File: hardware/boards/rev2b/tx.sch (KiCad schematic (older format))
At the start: 59 parts, among them J3 SMA, Q2 RE1C002UN, T1 uwave, T2 uwave, U12 ADF4158, U13 TLV172DCK, U14 PAT1220-C-3DB, U15 HMC431, U16 PD4859J5050S2HF, U17 PAT1220-C-5DB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

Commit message: rev2b pcb: replace wilkinson divider with power splitter
Closes #4.
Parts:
- removed R47: 100, fmcw_v5:R_0603b, symbol Device:R
- removed U14: PAT1220-C-3DB, RF_Converter:RF_Attenuator_Susumu_PAT1220, symbol RF:PAT1220-C-3DB
- removed U16: PD4859J5050S2HF, RF_Converter:Anaren_0805_2012Metric-6, symbol RF:PD4859J5050S2HF
- added U14: PS2012GT2-R50, fmcw_v5:Susumu_PS2012GT2-R50, symbol fmcw:PS2012GT2-R50
- U17: value PAT1220-C-5DB -> PAT1220-C-2DB; symbol RF:PAT1220-C-5DB -> RF:PAT1220-C-2DB; MFN PAT1220-C-5DB-T5 -> PAT1220-C-2DB-T5
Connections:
- net GND: now also U14.4 (GND)
- net at U15.16 (RFOUT): now also U14.1 (In)
- net at C112.1: now also T1.1, T2.1, U14.3 (Out)
- net at U17.1: now also U14.2 (Out)
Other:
- note removed: "-1 dBm"
- moved on the sheet: T2
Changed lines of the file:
@@
 Connection ~ 3050 5550
 Connection ~ 6800 6000
-Connection ~ 9950 5800
-Connection ~ 9950 6200
 Connection ~ 8150 5050
 Connection ~ 6200 5550
@@
 Connection ~ 8150 6400
 Connection ~ 9300 7450
-Connection ~ 9950 7150
 NoConn ~ 2900 5800
 NoConn ~ 12500 4800
@@
 	4000 6700 4000 6650
 Wire Wire Line
-	4400 7450 7400 7450
-Wire Wire Line
 	4450 4000 4300 4000
 Wire Wire Line
@@
 	7750 6400 8150 6400
 Wire Wire Line
-	7800 7850 7800 7900
-Wire Wire Line
 	7850 3800 7900 3800
 Wire Wire Line
@@
 	8200 5250 8150 5250
 Wire Wire Line
-	8200 7450 9300 7450
-Wire Wire Line
 	8250 3550 8250 3600
 Wire Wire Line
@@
 	9300 7450 9300 7550
 Wire Wire Line
-	9300 7450 9950 7450
-Wire Wire Line
-	9400 6350 9400 6300
+	9300 7450 10150 7450
 Wire Wire Line
 	9450 3550 9450 2900
@@
 	9550 3550 9450 3550
 Wire Wire Line
-	9800 5900 9850 5900
-Wire Wire Line
-	9800 6100 9850 6100
-Wire Wire Line
 	9850 4100 9950 4100
 Wire Wire Line
-	9850 5800 9850 5900
-Wire Wire Line
-	9850 6100 9850 6200
-Wire Wire Line
-	9850 6200 9950 6200
-Wire Wire Line
 	9950 3550 9850 3550
 Wire Wire Line
@@
 	9950 4450 9800 4450
 Wire Wire Line
-	9950 5100 9950 5800
-Wire Wire Line
 	9950 5100 10000 5100
 Wire Wire Line
-	9950 5800 9850 5800
-Wire Wire Line
-	9950 5800 9950 5850
-Wire Wire Line
-	9950 6150 9950 6200
-Wire Wire Line
-	9950 6200 9950 7150
-Wire Wire Line
-	9950 7150 9950 7450
+	10150 7150 10150 7450
 Wire Wire Line
 	10050 4100 10050 4300
@@
 Text Notes 1200 4700 0    50   ~ 0
 32 (23) mA
-Text Notes 3200 7450 0    50   ~ 0
--4 dBm
 Text Notes 4900 4250 2    50   ~ 0
 5 mA
@@
 +2dBm
 Text Notes 8850 7450 0    50   ~ 0
--1 dBm
+-4 dBm
 Text Notes 9000 4000 0    50   ~ 0
 2.85V
 Text Notes 9600 5400 0    50   ~ 0
--1 dBm
+-4 dBm
 Text Notes 9900 2050 0    50   ~ 0
 800 (300) mA
@@
 $EndComp
 $Comp
-L power:GND #PWR0115
-U 1 1 5CF6E09E
-P 7800 7900
-F 0 "#PWR0115" H 7800 7650 50  0001 C CNN
-F 1 "GND" H 7805 7727 50  0000 C CNN
-F 2 "" H 7800 7900 50  0001 C CNN
-F 3 "" H 7800 7900 50  0001 C CNN
-	1    7800 7900
-	1    0    0    -1
-$EndComp
-$Comp
 L power:GND #PWR0101
 U 1 1 5C609590
@@
 L power:GND #PWR0121
 U 1 1 5CE085DA
-P 9400 6350
-F 0 "#PWR0121" H 9400 6100 50  0001 C CNN
-F 1 "GND" H 9405 6177 50  0000 C CNN
-F 2 "" H 9400 6350 50  0001 C CNN
-F 3 "" H 9400 6350 50  0001 C CNN
-	1    9400 6350
+P 9200 6450
+F 0 "#PWR0121" H 9200 6200 50  0001 C CNN
+F 1 "GND" H 9205 6277 50  0000 C CNN
+F 2 "" H 9200 6450 50  0001 C CNN
+F 3 "" H 9200 6450 50  0001 C CNN
+	1    9200 6450
 	1    0    0    -1
 $EndComp
@@
 $EndComp
 $Comp
-L Device:R R47
-U 1 1 5CFA8165
-P 9950 6000
-F 0 "R47" H 10020 6046 50  0000 L CNN
-F 1 "100" H 10020 5955 50  0000 L CNN
-F 2 "fmcw_v5:R_0603b" V 9880 6000 50  0001 C CNN
-F 3 "~" H 9950 6000 50  0001 C CNN
-F 4 "" H 9950 6000 50  0001 C CNN "MFN"
-	1    9950 6000
-	1    0    0    -1
-$EndComp
-$Comp
 L Device:R R114
 U 1 1 5E79D780
@@
 L fmcw:uwave T2
 U 1 1 5EB0CF7E
-P 10100 7150
-F 0 "T2" V 10055 7278 50  0000 L CNN
-F 1 "uwave" V 10145 7278 50  0000 L CNN
-F 2 "fmcw_v5:uwm_0.38_0.17_90" H 10100 7150 50  0001 C CNN
-F 3 "" H 10100 7150 50  0001 C CNN
-	1    10100 7150
+P 10300 7150
+F 0 "T2" V 10255 7278 50  0000 L CNN
+F 1 "uwave" V 10345 7278 50  0000 L CNN
+F 2 "fmcw_v5:uwm_0.38_0.17_90" H 10300 7150 50  0001 C CNN
+F 3 "" H 10300 7150 50  0001 C CNN
+	1    10300 7150
 	0    1    1    0
 $EndComp
@@
 $EndComp
 $Comp
-L RF:PAT1220-C-3DB U14
-U 1 1 5CF46E5A
-P 7800 7550
-AR Path="/5CF46E5A" Ref="U14"  Part="1"
-AR Path="/59396B94/5CF46E5A" Ref="U14"  Part="1"
-F 0 "U14" H 7800 7939 60  0000 C CNN
-F 1 "PAT1220-C-3DB" H 7800 7833 60  0000 C CNN
-F 2 "RF_Converter:RF_Attenuator_Susumu_PAT1220" H 7800 7550 60  0001 C CNN
-F 3 "" H 7800 7550 60  0000 C CNN
-F 4 "PAT1220-C-3DB-T5" H -3400 2550 50  0001 C CNN "MFN"
-	1    7800 7550
-	1    0    0    -1
-$EndComp
-$Comp
-L RF:PD4859J5050S2HF U16
-U 1 1 5CDBB6B7
-P 9400 6000
-F 0 "U16" H 9400 6367 50  0000 C CNN
-F 1 "PD4859J5050S2HF" H 9400 6276 50  0000 C CNN
-F 2 "RF_Converter:Anaren_0805_2012Metric-6" H 9400 5600 50  0001 C CNN
-F 3 "" H 9150 6250 50  0001 C CNN
-F 4 "PD4859J5050S2HF" H 9400 6000 50  0001 C CNN "MFN"
-	1    9400 6000
-	1    0    0    -1
-$EndComp
-$Comp
-L RF:PAT1220-C-5DB U17
+L RF:PAT1220-C-2DB U17
 U 1 1 54FB1677
 P 10400 5200
@@
 AR Path="/59396B94/54FB1677" Ref="U17"  Part="1"
 F 0 "U17" H 10150 4900 60  0000 C CNN
-F 1 "PAT1220-C-5DB" H 10800 4900 60  0000 C CNN
+F 1 "PAT1220-C-2DB" H 10800 4900 60  0000 C CNN
 F 2 "RF_Converter:RF_Attenuator_Susumu_PAT1220" H 10400 5200 60  0001 C CNN
 F 3 "" H 10400 5200 60  0000 C CNN
-F 4 "PAT1220-C-5DB-T5" H -800 200 50  0001 C CNN "MFN"
+F 4 "PAT1220-C-2DB-T5" H -800 200 50  0001 C CNN "MFN"
 	1    10400 5200
 	1    0    0    -1
@@
 	1    0    0    -1
 $EndComp
+$Comp
+L fmcw:PS2012GT2-R50 U14
+U 1 1 5F5CD072
+P 9400 6000
+F 0 "U14" H 9400 6425 50  0000 C CNN
+F 1 "PS2012GT2-R50" H 9400 6334 50  0000 C CNN
+F 2 "fmcw_v5:Susumu_PS2012GT2-R50" H 9250 5550 50  0001 C CNN
+F 3 "https://www.susumu.co.jp/common/pdf/n_catalog_partition31_en.pdf" H 9350 5650 50  0001 C CNN
+	1    9400 6000
+	1    0    0    -1
+$EndComp
+Connection ~ 10150 7150
+Wire Wire Line
+	9200 6450 9200 6400
+Wire Wire Line
+	4400 7450 9300 7450
+Wire Wire Line
+	10150 5800 9800 5800
+Wire Wire Line
+	10150 5800 10150 7150
+Wire Wire Line
+	9950 6200 9800 6200
+Wire Wire Line
+	9950 5100 9950 6200
 $EndSCHEMATC

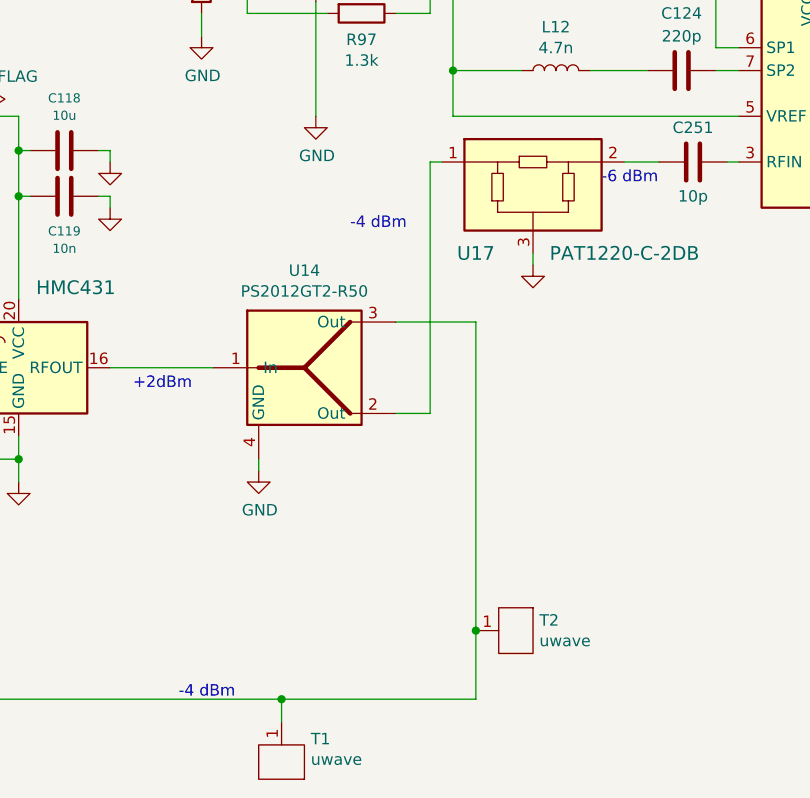
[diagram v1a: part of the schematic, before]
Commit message: rev2 pcb: finish routing traces
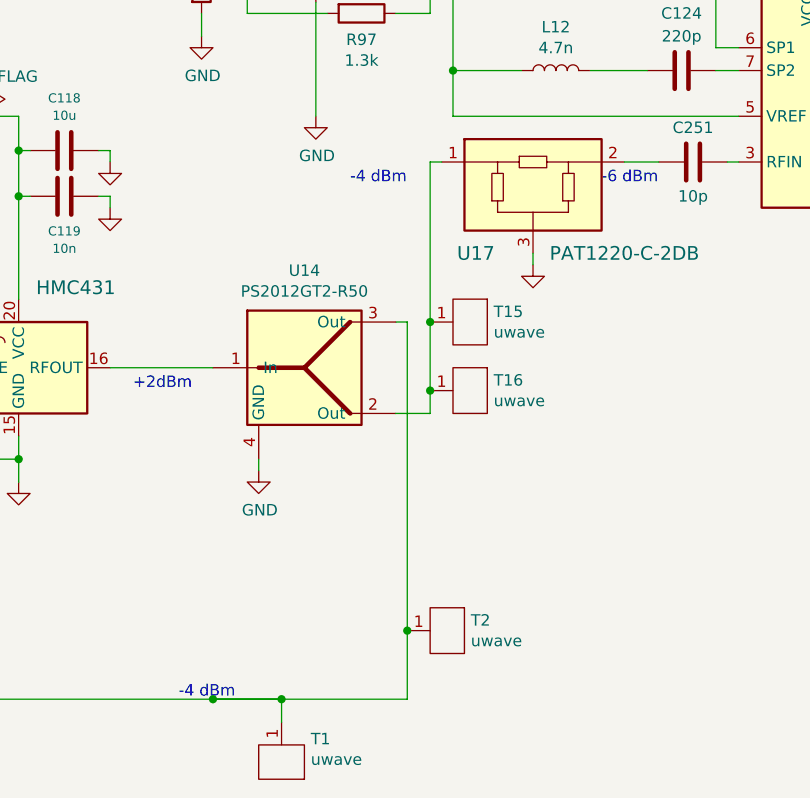
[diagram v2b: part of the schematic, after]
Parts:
- added T15, T16: uwave, fmcw_v5:uwm_0.38_0.17_90, symbol fmcw:uwave
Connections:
- net at U14.2 (Out), U17.1: now also T15.1, T16.1
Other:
- moved on the sheet: T2
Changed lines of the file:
@@
 	9300 7450 9300 7550
 Wire Wire Line
-	9300 7450 10150 7450
-Wire Wire Line
 	9450 3550 9450 2900
 Wire Wire Line
@@
 	9950 5100 10000 5100
 Wire Wire Line
-	10150 7150 10150 7450
+	9850 7150 9850 7450
 Wire Wire Line
 	10050 4100 10050 4300
@@
 Text Notes 9000 4000 0    50   ~ 0
 2.85V
-Text Notes 9600 5400 0    50   ~ 0
+Text Notes 9600 5200 0    50   ~ 0
 -4 dBm
 Text Notes 9900 2050 0    50   ~ 0
@@
 L fmcw:uwave T2
 U 1 1 5EB0CF7E
-P 10300 7150
-F 0 "T2" V 10255 7278 50  0000 L CNN
-F 1 "uwave" V 10345 7278 50  0000 L CNN
-F 2 "fmcw_v5:uwm_0.38_0.17_90" H 10300 7150 50  0001 C CNN
-F 3 "" H 10300 7150 50  0001 C CNN
-	1    10300 7150
+P 10000 7150
+F 0 "T2" V 9955 7278 50  0000 L CNN
+F 1 "uwave" V 10045 7278 50  0000 L CNN
+F 2 "fmcw_v5:uwm_0.38_0.17_90" H 10000 7150 50  0001 C CNN
+F 3 "" H 10000 7150 50  0001 C CNN
+	1    10000 7150
 	0    1    1    0
 $EndComp
@@
 	1    0    0    -1
 $EndComp
-Connection ~ 10150 7150
+Connection ~ 9850 7150
 Wire Wire Line
 	9200 6450 9200 6400
 Wire Wire Line
+	9850 5800 9800 5800
+Wire Wire Line
+	9850 5800 9850 7150
+Wire Wire Line
+	9950 6200 9800 6200
+Wire Wire Line
+	9950 5100 9950 5800
+Connection ~ 9000 7450
+Wire Wire Line
+	9000 7450 9300 7450
+Wire Wire Line
+	9300 7450 9850 7450
+Wire Wire Line
 	4400 7450 9300 7450
-Wire Wire Line
-	10150 5800 9800 5800
-Wire Wire Line
-	10150 5800 10150 7150
-Wire Wire Line
-	9950 6200 9800 6200
-Wire Wire Line
-	9950 5100 9950 6200
+$Comp
+L fmcw:uwave T16
+U 1 1 5F968A43
+P 10100 6100
+F 0 "T16" V 10055 6228 50  0000 L CNN
+F 1 "uwave" V 10145 6228 50  0000 L CNN
+F 2 "fmcw_v5:uwm_0.38_0.17_90" H 10100 6100 50  0001 C CNN
+F 3 "" H 10100 6100 50  0001 C CNN
+	1    10100 6100
+	0    1    1    0
+$EndComp
+Connection ~ 9950 6100
+Wire Wire Line
+	9950 6100 9950 6200
+$Comp
+L fmcw:uwave T15
+U 1 1 5F968E22
+P 10100 5800
+F 0 "T15" V 10055 5928 50  0000 L CNN
+F 1 "uwave" V 10145 5928 50  0000 L CNN
+F 2 "fmcw_v5:uwm_0.38_0.17_90" H 10100 5800 50  0001 C CNN
+F 3 "" H 10100 5800 50  0001 C CNN
+	1    10100 5800
+	0    1    1    0
+$EndComp
+Connection ~ 9950 5800
+Wire Wire Line
+	9950 5800 9950 6100
 $EndSCHEMATC
